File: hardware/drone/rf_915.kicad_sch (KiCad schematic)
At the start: 1 part, among them U2 SX1262IMLTRT

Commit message: more radio work
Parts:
- added C46: 47p, symbol Device:C
- added C47: 47n, symbol Device:C
- added C48: 3p, symbol Device:C
- added C49, C55, C58, C59, C60: C, symbol Device:C
- added C50: 5.6p, symbol Device:C
- added C51: 39p, symbol Device:C
- added C52: 1.8p, symbol Device:C
- added C53: 1.8, symbol Device:C
- added C54: 2.4p, symbol Device:C
- added C56: 470n, symbol Device:C
- added C57: 1u, symbol Device:C
- added C61: 1n, symbol Device:C
- added C64, C65: 100n, symbol Device:C
- added L10: 15n, symbol Device:L
- added L11: 15u, symbol Device:L
- added L12: L, symbol Device:L
- added L6: 0R, symbol Device:L
- added L7: 47n, symbol Device:L
- added L8: 2.5n, symbol Device:L
- added L9: 4.7n, symbol Device:L
- added R8: 100R, symbol Device:R
- added U10: PE4259, symbol SoftDrone:PE4259
- added Y2: Crystal_GND24, symbol Device:Crystal_GND24
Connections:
- net VDD3V3: now reaches U2.1 (VDD_IN)
- net VDD3V3: now also U2.10 (VBAT), C57.1, C64.1
- net VDD1V8: now reaches U2.11 (VBAT_IO)
- net VDD1V8: now also C65.1
- net SX_DIO2: now reaches U2.12 (DIO2)
- net SX_DIO2: now also R8.1
- net SX_IRQ: now reaches U2.13 (DIO1)
- net SX_BUSY: now reaches U2.14 (BUSY)
- net SX_SPI5_MISO: now reaches U2.16 (MISO)
- net SX_SPI5_MOSI: now reaches U2.17 (MOSI)
- net SX_SPI5_SCK: now reaches U2.18 (SCK)
- net SX_SPI5_NSS: now reaches U2.19 (NSS)
- net GND: now reaches U2.2 (GND), U2.20 (GND), U2.25 (GND), U2.5 (GND), U2.8 (GND)
- net GND: now also C46.2, C47.2, C49.2, C50.2, C52.1, C53.1, C55.2, C56.2, C57.2, C59.1, C60.1, C61.1, C64.2, C65.2, U10.2 (GND), Y2.2 (G), Y2.4 (G)
- net at U2.21 (RFI_P): now also C53.2, L10.1
- net at U2.22 (RFI_N): now also C54.2, L10.2
- net at U2.23 (RFO): now also L6.1
- net at U2.24 (VR_PA): now also C46.1, C47.1, L7.2
- net at U2.3 (XTA): now also Y2.3
- net at U2.4 (XTB): now also Y2.1
- net at U2.7 (VREG): now also C56.1, L11.2
- net at U2.9 (DCC_SW): now also L11.1
- new net: C61.2, R8.2, U10.4 (CTRL)
- new net: C54.1, C55.1, U10.3 (RF2)
- new net: C48.1, C49.1, L6.2, L7.1, L8.1
- new net: C58.2, C59.2, L12.1
- new net: C60.2, L12.2
- new net: C48.2, C50.1, C51.1, L8.2
- new net: C51.2, L9.1
- new net: C52.2, L9.2, U10.1 (RF1)
- new net: C58.1, U10.5 (RFC)
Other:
- note added: "NRESET References VBAT"
- moved on the sheet: U2

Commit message: Finished GNSS, did more pinmuxxing
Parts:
- removed C49, C55: C, symbol Device:C
- added AE2: Antenna, Package_LCC:PLCC-84_29.3x29.3mm_P1.27mm, symbol Device:Antenna
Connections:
- net at C60.2, L12.2: now also AE2.1 (A)

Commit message: Added SWD
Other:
- note added: "SX1262 915MHz Radio"
- moved on the sheet: AE2, C46, C47, C48, C50, C51, C52, C53, C54, C56, C57, C58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

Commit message: Created pinmux table and completed pinmuxing
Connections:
- net SX_NRST: now reaches U2.15 (~{RESET})
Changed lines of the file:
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@@
+	(wire
+		(pts
+			(xy 44.45 71.12) (xy 49.53 71.12)
+		)
+		(stroke
+			(width 0)
+			(type default)
+		)
+	)
 	(wire
 		(pts
@@
 		)
 	)
+	(global_label "SX_NRST"
+		(shape input)
+		(at 44.45 71.12 180)
+		(fields_autoplaced yes)
+		(effects
+			(font
+				(size 1.27 1.27)
+			)
+			(justify right)
+		)
+		(property "Intersheetrefs" "${INTERSHEET_REFS}"
+			(at 33.3006 71.12 0)
+			(hide yes)
+			(show_name no)
+			(do_not_autoplace no)
+			(effects
+				(font
+					(size 1.27 1.27)
+				)
+				(justify right)
+			)
+		)
+	)

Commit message: Small cleanup
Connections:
- no-connect marks 0 -> 1
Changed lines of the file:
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@@
 		(color 0 0 0 0)
+	)
+	(no_connect
+		(at 49.53 83.82)
 	)
 	(wire

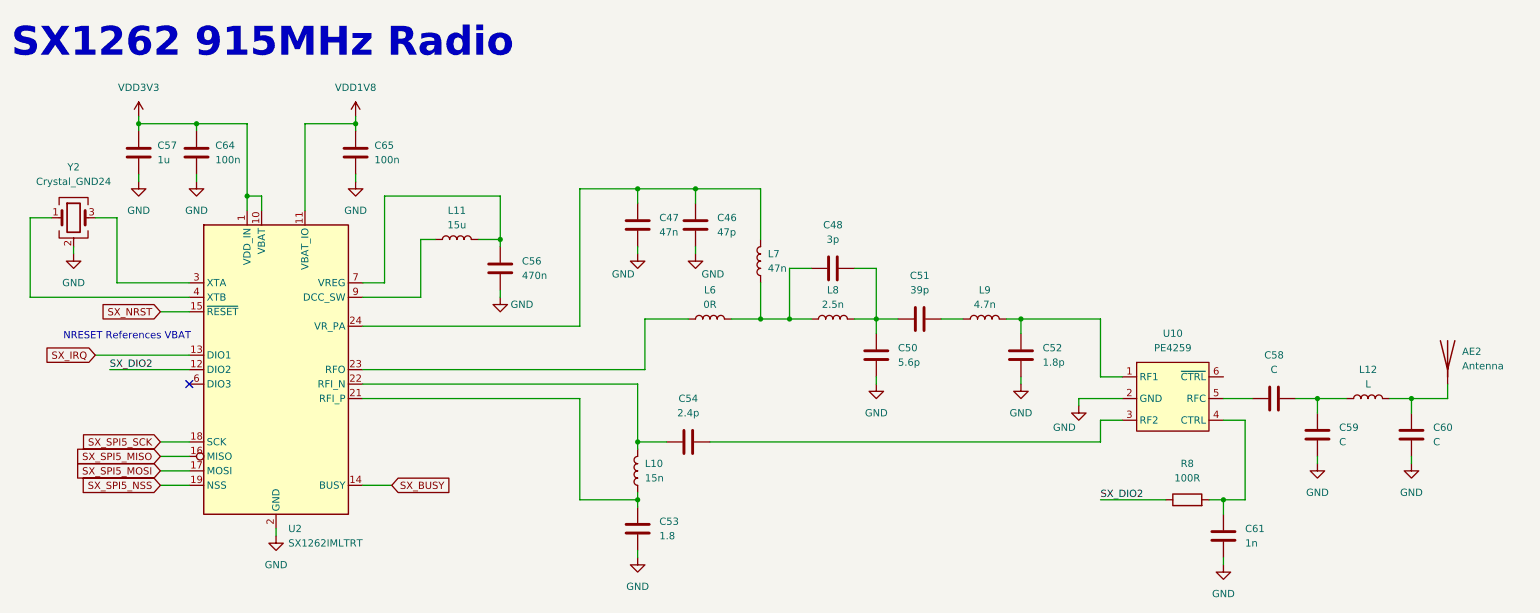
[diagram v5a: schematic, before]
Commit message: Added easier RF tuning setup with MM8030
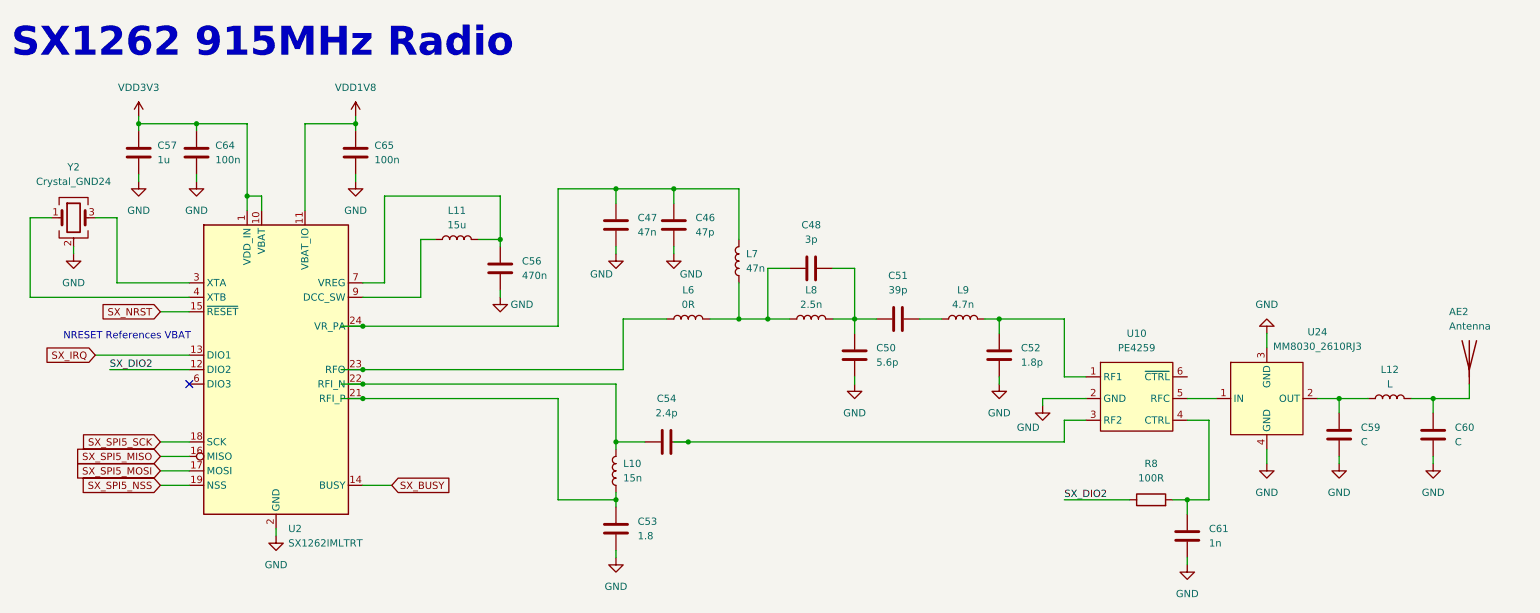
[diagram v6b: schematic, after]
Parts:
- removed C58: C, symbol Device:C
- added U24: MM8030_2610RJ3, symbol SoftDrone:MM8030_2610RJ3
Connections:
- net GND: now also U24.3 (GND), U24.4 (GND)
- net at C59.2, L12.1: now also U24.2 (OUT)
- net at U10.5 (RFC): now also U24.1 (IN)
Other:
- moved on the sheet: AE2, C46, C47, C48, C50, C51, C52, C53, C54, C59, C60, C61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

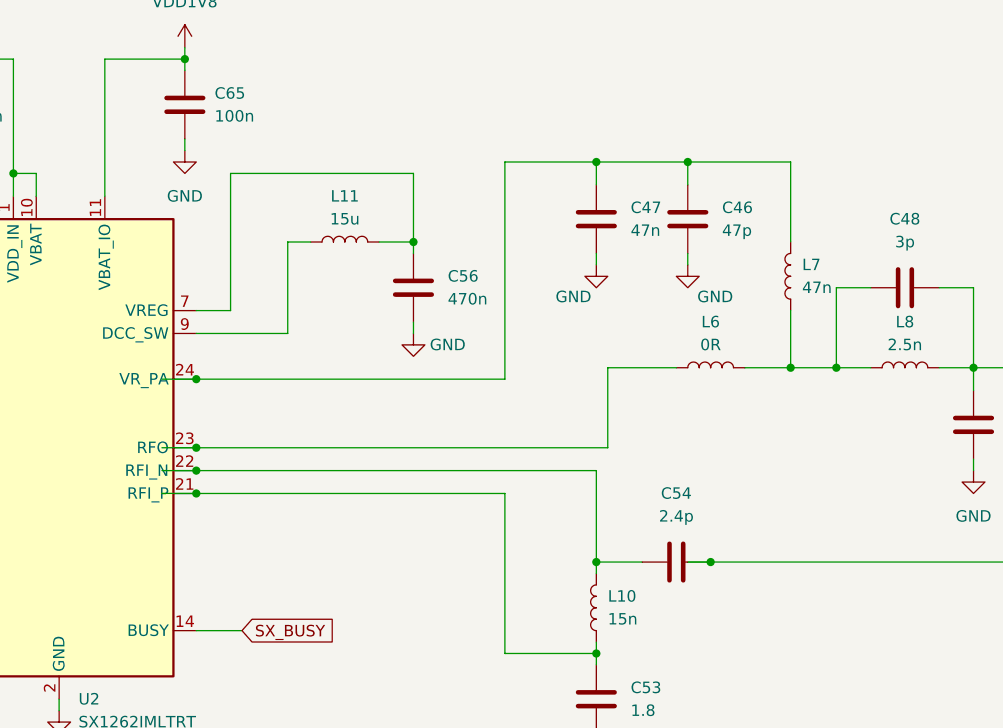
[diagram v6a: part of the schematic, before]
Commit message: Fixed some pullups and pinmuxxed more
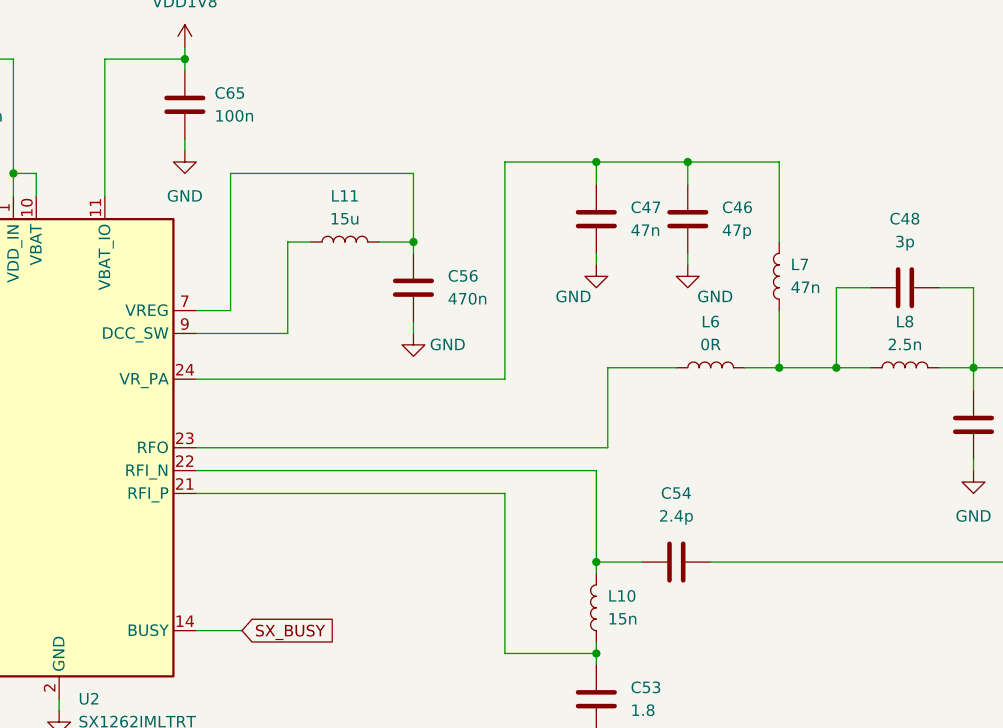
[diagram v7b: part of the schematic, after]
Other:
- moved on the sheet: L7
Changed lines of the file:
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@@
-	)
-	(junction
-		(at 137.16 93.98)
-		(diameter 0)
-		(color 0 0 0 0)
 	)
 	(junction
@@
 	)
 	(junction
-		(at 80.01 83.82)
-		(diameter 0)
-		(color 0 0 0 0)
-	)
-	(junction
-		(at 80.01 73.66)
-		(diameter 0)
-		(color 0 0 0 0)
-	)
-	(junction
 		(at 59.69 50.8)
-		(diameter 0)
-		(color 0 0 0 0)
-	)
-	(junction
-		(at 80.01 86.36)
 		(diameter 0)
 		(color 0 0 0 0)
@@
 	)
 	(junction
-		(at 80.01 81.28)
-		(diameter 0)
-		(color 0 0 0 0)
-	)
-	(junction
 		(at 124.46 104.14)
 		(diameter 0)
@@
 	)
 	(junction
-		(at 146.05 72.39)
+		(at 144.78 72.39)
 		(diameter 0)
 		(color 0 0 0 0)
@@
 	(wire
 		(pts
-			(xy 76.2 73.66) (xy 80.01 73.66)
-		)
-		(stroke
-			(width 0)
-			(type default)
-		)
-	)
-	(wire
-		(pts
 			(xy 44.45 93.98) (xy 49.53 93.98)
 		)
@@
 	(wire
 		(pts
-			(xy 76.2 86.36) (xy 80.01 86.36)
-		)
-		(stroke
-			(width 0)
-			(type default)
-		)
-	)
-	(wire
-		(pts
 			(xy 83.82 50.8) (xy 104.14 50.8)
 		)
@@
 	(wire
 		(pts
-			(xy 146.05 49.53) (xy 134.62 49.53)
+			(xy 144.78 49.53) (xy 134.62 49.53)
 		)
 		(stroke
@@
 	(wire
 		(pts
-			(xy 76.2 83.82) (xy 80.01 83.82)
-		)
-		(stroke
-			(width 0)
-			(type default)
-		)
-	)
-	(wire
-		(pts
 			(xy 29.21 59.69) (xy 29.21 60.96)
 		)
@@
 	(wire
 		(pts
-			(xy 134.62 93.98) (xy 137.16 93.98)
-		)
-		(stroke
-			(width 0)
-			(type default)
-		)
-	)
-	(wire
-		(pts
 			(xy 267.97 96.52) (xy 267.97 97.79)
 		)
@@
 	(wire
 		(pts
-			(xy 146.05 66.04) (xy 146.05 72.39)
+			(xy 144.78 66.04) (xy 144.78 72.39)
 		)
 		(stroke
@@
 	(wire
 		(pts
-			(xy 146.05 58.42) (xy 146.05 49.53)
-		)
-		(stroke
-			(width 0)
-			(type default)
-		)
-	)
-	(wire
-		(pts
-			(xy 146.05 72.39) (xy 151.13 72.39)
+			(xy 144.78 58.42) (xy 144.78 49.53)
 		)
 		(stroke
@@
 	(wire
 		(pts
-			(xy 76.2 81.28) (xy 80.01 81.28)
-		)
-		(stroke
-			(width 0)
-			(type default)
-		)
-	)
-	(wire
-		(pts
 			(xy 59.69 38.1) (xy 59.69 50.8)
 		)
@@
 	(wire
 		(pts
-			(xy 146.05 72.39) (xy 140.97 72.39)
+			(xy 140.97 72.39) (xy 151.13 72.39)
 		)
 		(stroke
@@
 	(symbol
 		(lib_id "Device:L")
-		(at 146.05 62.23 180)
+		(at 144.78 62.23 180)
 		(unit 1)
 		(body_style 1)
@@
 		(fields_autoplaced yes)
 		(property "Reference" "L7"
-			(at 147.32 60.9599 0)
+			(at 146.05 60.9599 0)
 			(show_name no)
 			(do_not_autoplace no)
@@
 		)
 		(property "Value" "47n"
-			(at 147.32 63.4999 0)
+			(at 146.05 63.4999 0)
 			(show_name no)
 			(do_not_autoplace no)
@@
 		)
 		(property "Footprint" ""
-			(at 146.05 62.23 0)
+			(at 144.78 62.23 0)
 			(hide yes)
 			(show_name no)
@@
 		)
 		(property "Datasheet" ""
-			(at 146.05 62.23 0)
+			(at 144.78 62.23 0)
 			(hide yes)
 			(show_name no)
@@
 		)
 		(property "Description" "Inductor"
-			(at 146.05 62.23 0)
-			(hide yes)
-			(show_name no)
+			(at 144.78 62.23 0)
+			(hide yes)
+			(show_name no)

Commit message: Started footprint assignments
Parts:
- AE2: footprint Package_LCC:PLCC-84_29.3x29.3mm_P1.27mm -> (none)
- U10: footprint (none) -> PE4259-63:SOT65P210X110-6N
- U2: footprint Package_DFN_QFN:QFN-24-1EP_4x4mm_P0.5mm_EP2.6x2.6mm -> Package_DFN_QFN:QFN-24-1EP_4x4mm_P0.5mm_EP2.7x2.7mm
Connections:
- net VDD1V8: now also U10.6 (~{CTRL})
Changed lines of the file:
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@@
 	(wire
 		(pts
+			(xy 227.33 78.74) (xy 227.33 82.55)
+		)
+		(stroke
+			(width 0)
+			(type default)
+		)
+	)
+	(wire
+		(pts
 			(xy 114.3 73.66) (xy 114.3 49.53)
 		)
@@
 	(wire
 		(pts
+			(xy 227.33 82.55) (xy 224.79 82.55)
+		)
+		(stroke
+			(width 0)
+			(type default)
+		)
+	)
+	(wire
+		(pts
 			(xy 151.13 72.39) (xy 154.94 72.39)
 		)
@@
 	)
 	(symbol
+		(lib_id "power:VDD")
+		(at 227.33 78.74 0)
+		(unit 1)
+		(body_style 1)
+		(exclude_from_sim no)
+		(in_bom yes)
+		(on_board yes)
+		(in_pos_files yes)
+		(dnp no)
+		(fields_autoplaced yes)
+		(property "Reference" "#PWR0217"
+			(at 227.33 82.55 0)
+			(hide yes)
+			(show_name no)
+			(do_not_autoplace no)
+			(effects
+				(font
+					(size 1.27 1.27)
+				)
+			)
+		)
+		(property "Value" "VDD1V8"
+			(at 227.33 73.66 0)
+			(show_name no)
+			(do_not_autoplace no)
+			(effects
+				(font
+					(size 1.27 1.27)
+				)
+			)
+		)
+		(property "Footprint" ""
+			(at 227.33 78.74 0)
+			(hide yes)
+			(show_name no)
+			(do_not_autoplace no)
+			(effects
+				(font
+					(size 1.27 1.27)
+				)
+			)
+		)
+		(property "Datasheet" ""
+			(at 227.33 78.74 0)
+			(hide yes)
+			(show_name no)
+			(do_not_autoplace no)
+			(effects
+				(font
+					(size 1.27 1.27)
+				)
+			)
+		)
+		(property "Description" "Power symbol creates a global label with name \"VDD\""
+			(at 227.33 78.74 0)
+			(hide yes)
+			(show_name no)
+			(do_not_autoplace no)
+			(effects
+				(font
+					(size 1.27 1.27)
+				)
+			)
+		)
+		(pin "1"
+		)
+		(instances
+			(project "drone"
+				(path "/62c402a6-ed3f-446b-8423-821e9cc6908b/65bc9e57-6095-4efd-893a-5e1083f61580"
+					(reference "#PWR0217")
+					(unit 1)
+				)
+			)
+		)
+	)
+	(symbol
 		(lib_id "Device:C")
 		(at 40.64 43.18 0)
@@
 			)
 		)
-		(property "Footprint" "Package_DFN_QFN:QFN-24-1EP_4x4mm_P0.5mm_EP2.6x2.6mm"
+		(property "Footprint" "Package_DFN_QFN:QFN-24-1EP_4x4mm_P0.5mm_EP2.7x2.7mm"
 			(at 66.04 113.03 0)
 			(hide yes)
@@
 			)
 		)
-		(property "Footprint" "Package_LCC:PLCC-84_29.3x29.3mm_P1.27mm"
+		(property "Footprint" ""
 			(at 274.32 78.74 0)
 			(hide yes)
@@
 			)
 		)
-		(property "Footprint" ""
+		(property "Footprint" "PE4259-63:SOT65P210X110-6N"
 			(at 215.9 86.36 0)
 			(hide yes)
